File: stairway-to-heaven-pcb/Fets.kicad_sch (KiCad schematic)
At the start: 12 parts, among them Q1 FDN337N, Q2 FDN337N, Q3 FDN337N, Q4 FDN337N, Q5 FDN337N, Q6 FDN337N

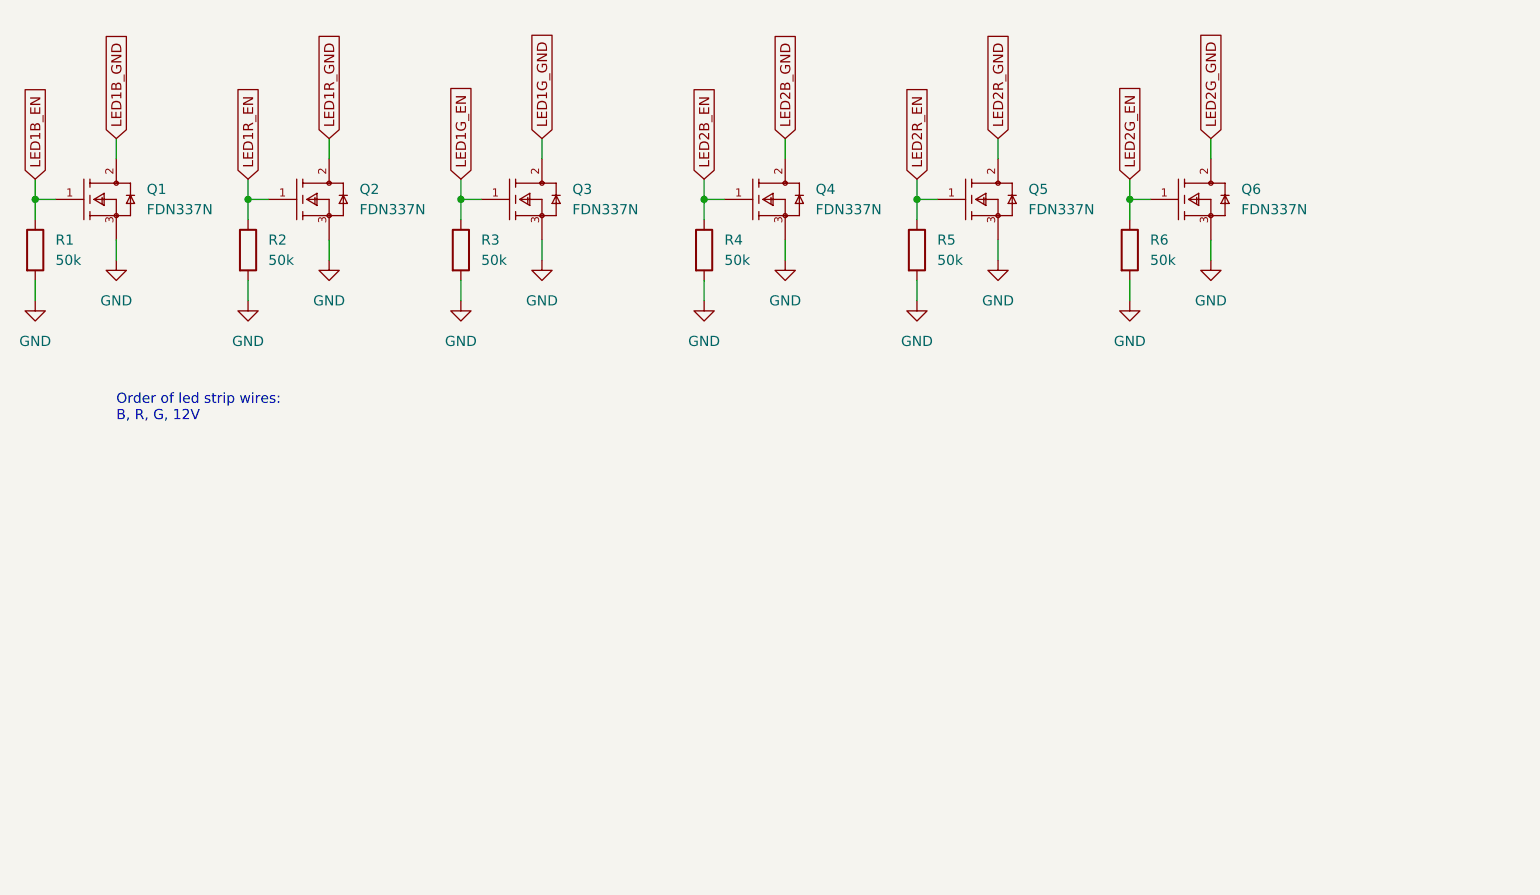
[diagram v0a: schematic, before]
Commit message: Psu, hierachical pages for fet driver
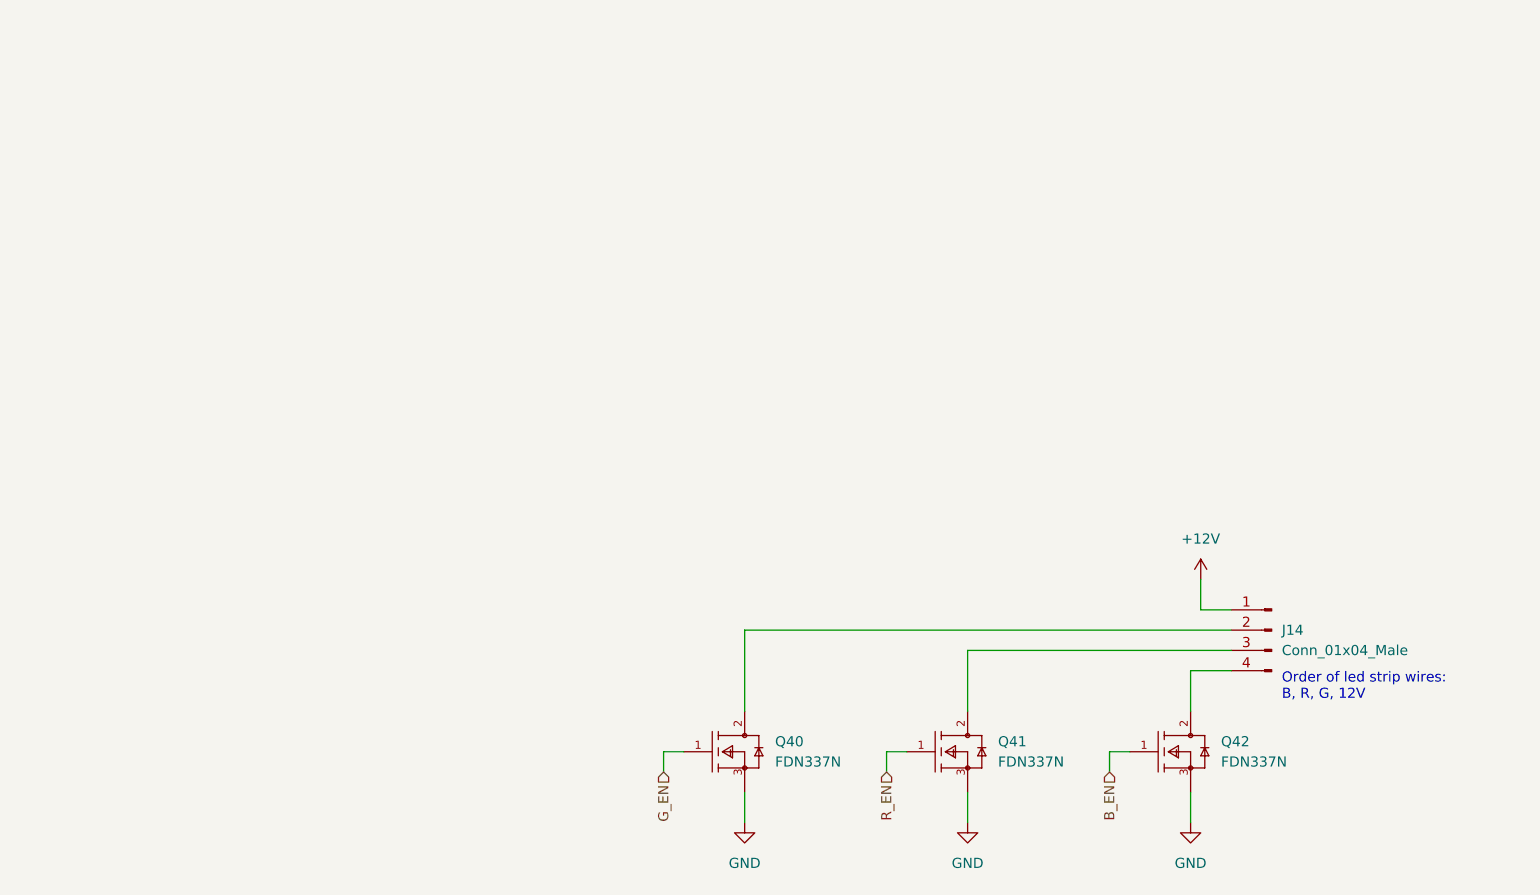
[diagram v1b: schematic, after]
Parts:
- removed Q1, Q2, Q3, Q4, Q5, Q6: FDN337N, FDN337N:ON_Semi-527AG-01-12_2008-O-IPC_B, symbol FDN337N:FDN337N
- removed R1, R2, R3, R4, R5, R6: 50k, Resistor_SMD:R_0805_2012Metric, symbol Device:R
- added J14: Conn_01x04_Male, Connector_PinHeader_2.54mm:PinHeader_1x04_P2.54mm_Vertical, symbol Connector:Conn_01x04_Male
- added Q40, Q41, Q42: FDN337N, FDN337N:ON_Semi-527AG-01-12_2008-O-IPC_B, symbol FDN337N:FDN337N
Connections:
- net GND: now also Q40.3 (S), Q41.3 (S), Q42.3 (S)
- new net: J14.2 (Pin_2), Q40.2 (D)
- new net: J14.4 (Pin_4), Q42.2 (D)
- new net: J14.3 (Pin_3), Q41.2 (D)
- new net +12V: J14.1 (Pin_1)
- new net B_EN: Q42.1 (G)
- new net G_EN: Q40.1 (G)
- new net R_EN: Q41.1 (G)

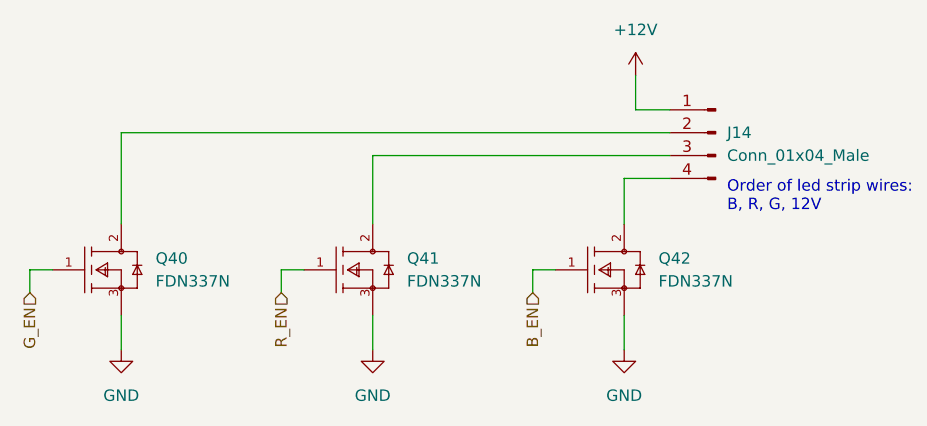
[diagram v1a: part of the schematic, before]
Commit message: initial pcb placement and routing tests
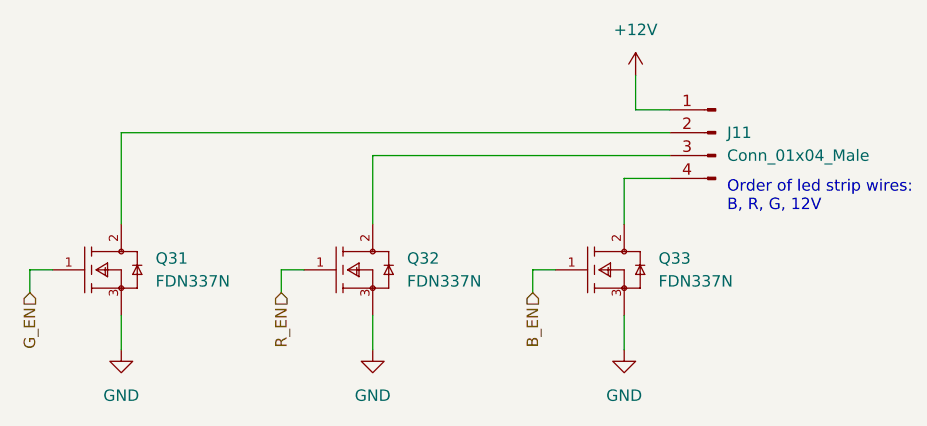
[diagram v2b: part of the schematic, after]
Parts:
- J11: renamed from J14; footprint Connector_PinHeader_2.54mm:PinHeader_1x04_P2.54mm_Vertical -> kicad-ss-libs:ScrewTerminal-5_08
- renumbered Q40 to Q31, Q41 to Q32, Q42 to Q33
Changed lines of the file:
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@@
   (symbol (lib_id "power:GND") (at 162.56 113.665 0)
     (in_bom yes) (on_board yes) (fields_autoplaced)
-    (property "Reference" "#PWR0157" (id 0) (at 162.56 120.015 0)
+    (property "Reference" "#PWR0145" (id 0) (at 162.56 120.015 0)
       (effects (font (size 1.27 1.27)) hide)
     )
@@
   (symbol (lib_id "FDN337N:FDN337N") (at 96.52 104.775 0)
     (in_bom yes) (on_board yes) (fields_autoplaced)
-    (property "Reference" "Q40" (id 0) (at 110.49 103.5049 0)
+    (property "Reference" "Q31" (id 0) (at 110.49 103.5049 0)
       (effects (font (size 1.27 1.27)) (justify left))
     )
@@
   (symbol (lib_id "FDN337N:FDN337N") (at 152.4 104.775 0)
     (in_bom yes) (on_board yes) (fields_autoplaced)
-    (property "Reference" "Q42" (id 0) (at 166.37 103.5049 0)
+    (property "Reference" "Q33" (id 0) (at 166.37 103.5049 0)
       (effects (font (size 1.27 1.27)) (justify left))
     )
@@
   (symbol (lib_id "power:GND") (at 134.62 113.665 0)
     (in_bom yes) (on_board yes) (fields_autoplaced)
-    (property "Reference" "#PWR0155" (id 0) (at 134.62 120.015 0)
+    (property "Reference" "#PWR0143" (id 0) (at 134.62 120.015 0)
       (effects (font (size 1.27 1.27)) hide)
     )
@@
   (symbol (lib_id "Connector:Conn_01x04_Male") (at 172.72 89.535 0) (mirror y)
     (in_bom yes) (on_board yes) (fields_autoplaced)
-    (property "Reference" "J14" (id 0) (at 173.99 89.5349 0)
+    (property "Reference" "J11" (id 0) (at 173.99 89.5349 0)
       (effects (font (size 1.27 1.27)) (justify right))
     )
@@
       (effects (font (size 1.27 1.27)) (justify right))
     )
-    (property "Footprint" "Connector_PinHeader_2.54mm:PinHeader_1x04_P2.54mm_Vertical" (id 2) (at 172.72 89.535 0)
+    (property "Footprint" "kicad-ss-libs:ScrewTerminal-5_08" (id 2) (at 172.72 89.535 0)
       (effects (font (size 1.27 1.27)) hide)
     )
@@
   (symbol (lib_id "FDN337N:FDN337N") (at 124.46 104.775 0)
     (in_bom yes) (on_board yes) (fields_autoplaced)
-    (property "Reference" "Q41" (id 0) (at 138.43 103.5049 0)
+    (property "Reference" "Q32" (id 0) (at 138.43 103.5049 0)
       (effects (font (size 1.27 1.27)) (justify left))
     )
@@
   (symbol (lib_id "power:GND") (at 106.68 113.665 0)
     (in_bom yes) (on_board yes) (fields_autoplaced)
-    (property "Reference" "#PWR0156" (id 0) (at 106.68 120.015 0)
+    (property "Reference" "#PWR0144" (id 0) (at 106.68 120.015 0)
       (effects (font (size 1.27 1.27)) hide)
     )
@@
   (symbol (lib_id "power:+12V") (at 163.83 83.185 0)
     (in_bom yes) (on_board yes) (fields_autoplaced)
-    (property "Reference" "#PWR0158" (id 0) (at 163.83 86.995 0)
-      (effects (font (size 1.27 1.27)) hide)
-    )
+    (property "Reference" "#PWR0146" (id 0) (at 163.83 86.995 0)
+      (effects (font (size 1.27 1.27)) hide)
+    )

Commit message: psu layout
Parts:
- renumbered J11 to J14, Q31 to Q40, Q32 to Q41, Q33 to Q42
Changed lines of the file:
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@@
   (symbol (lib_id "power:GND") (at 162.56 113.665 0)
     (in_bom yes) (on_board yes) (fields_autoplaced)
-    (property "Reference" "#PWR0145" (id 0) (at 162.56 120.015 0)
+    (property "Reference" "#PWR0157" (id 0) (at 162.56 120.015 0)
       (effects (font (size 1.27 1.27)) hide)
     )
@@
   (symbol (lib_id "FDN337N:FDN337N") (at 96.52 104.775 0)
     (in_bom yes) (on_board yes) (fields_autoplaced)
-    (property "Reference" "Q31" (id 0) (at 110.49 103.5049 0)
+    (property "Reference" "Q40" (id 0) (at 110.49 103.5049 0)
       (effects (font (size 1.27 1.27)) (justify left))
     )
@@
   (symbol (lib_id "FDN337N:FDN337N") (at 152.4 104.775 0)
     (in_bom yes) (on_board yes) (fields_autoplaced)
-    (property "Reference" "Q33" (id 0) (at 166.37 103.5049 0)
+    (property "Reference" "Q42" (id 0) (at 166.37 103.5049 0)
       (effects (font (size 1.27 1.27)) (justify left))
     )
@@
   (symbol (lib_id "power:GND") (at 134.62 113.665 0)
     (in_bom yes) (on_board yes) (fields_autoplaced)
-    (property "Reference" "#PWR0143" (id 0) (at 134.62 120.015 0)
+    (property "Reference" "#PWR0155" (id 0) (at 134.62 120.015 0)
       (effects (font (size 1.27 1.27)) hide)
     )
@@
   (symbol (lib_id "Connector:Conn_01x04_Male") (at 172.72 89.535 0) (mirror y)
     (in_bom yes) (on_board yes) (fields_autoplaced)
-    (property "Reference" "J11" (id 0) (at 173.99 89.5349 0)
+    (property "Reference" "J14" (id 0) (at 173.99 89.5349 0)
       (effects (font (size 1.27 1.27)) (justify right))
     )
@@
   (symbol (lib_id "FDN337N:FDN337N") (at 124.46 104.775 0)
     (in_bom yes) (on_board yes) (fields_autoplaced)
-    (property "Reference" "Q32" (id 0) (at 138.43 103.5049 0)
+    (property "Reference" "Q41" (id 0) (at 138.43 103.5049 0)
       (effects (font (size 1.27 1.27)) (justify left))
     )
@@
   (symbol (lib_id "power:GND") (at 106.68 113.665 0)
     (in_bom yes) (on_board yes) (fields_autoplaced)
-    (property "Reference" "#PWR0144" (id 0) (at 106.68 120.015 0)
+    (property "Reference" "#PWR0156" (id 0) (at 106.68 120.015 0)
       (effects (font (size 1.27 1.27)) hide)
     )
@@
   (symbol (lib_id "power:+12V") (at 163.83 83.185 0)
     (in_bom yes) (on_board yes) (fields_autoplaced)
-    (property "Reference" "#PWR0146" (id 0) (at 163.83 86.995 0)
-      (effects (font (size 1.27 1.27)) hide)
-    )
+    (property "Reference" "#PWR0158" (id 0) (at 163.83 86.995 0)
+      (effects (font (size 1.27 1.27)) hide)
+    )

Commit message: Vias galore
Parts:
- renumbered J14 to J4, Q40 to Q10, Q41 to Q11, Q42 to Q12
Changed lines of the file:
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@@
   (symbol (lib_id "power:GND") (at 162.56 113.665 0)
     (in_bom yes) (on_board yes) (fields_autoplaced)
-    (property "Reference" "#PWR0157" (id 0) (at 162.56 120.015 0)
+    (property "Reference" "#PWR0117" (id 0) (at 162.56 120.015 0)
       (effects (font (size 1.27 1.27)) hide)
     )
@@
   (symbol (lib_id "FDN337N:FDN337N") (at 96.52 104.775 0)
     (in_bom yes) (on_board yes) (fields_autoplaced)
-    (property "Reference" "Q40" (id 0) (at 110.49 103.5049 0)
+    (property "Reference" "Q10" (id 0) (at 110.49 103.5049 0)
       (effects (font (size 1.27 1.27)) (justify left))
     )
@@
   (symbol (lib_id "FDN337N:FDN337N") (at 152.4 104.775 0)
     (in_bom yes) (on_board yes) (fields_autoplaced)
-    (property "Reference" "Q42" (id 0) (at 166.37 103.5049 0)
+    (property "Reference" "Q12" (id 0) (at 166.37 103.5049 0)
       (effects (font (size 1.27 1.27)) (justify left))
     )
@@
   (symbol (lib_id "power:GND") (at 134.62 113.665 0)
     (in_bom yes) (on_board yes) (fields_autoplaced)
-    (property "Reference" "#PWR0155" (id 0) (at 134.62 120.015 0)
+    (property "Reference" "#PWR0115" (id 0) (at 134.62 120.015 0)
       (effects (font (size 1.27 1.27)) hide)
     )
@@
   (symbol (lib_id "Connector:Conn_01x04_Male") (at 172.72 89.535 0) (mirror y)
     (in_bom yes) (on_board yes) (fields_autoplaced)
-    (property "Reference" "J14" (id 0) (at 173.99 89.5349 0)
+    (property "Reference" "J4" (id 0) (at 173.99 89.5349 0)
       (effects (font (size 1.27 1.27)) (justify right))
     )
@@
   (symbol (lib_id "FDN337N:FDN337N") (at 124.46 104.775 0)
     (in_bom yes) (on_board yes) (fields_autoplaced)
-    (property "Reference" "Q41" (id 0) (at 138.43 103.5049 0)
+    (property "Reference" "Q11" (id 0) (at 138.43 103.5049 0)
       (effects (font (size 1.27 1.27)) (justify left))
     )
@@
   (symbol (lib_id "power:GND") (at 106.68 113.665 0)
     (in_bom yes) (on_board yes) (fields_autoplaced)
-    (property "Reference" "#PWR0156" (id 0) (at 106.68 120.015 0)
+    (property "Reference" "#PWR0116" (id 0) (at 106.68 120.015 0)
       (effects (font (size 1.27 1.27)) hide)
     )
@@
   (symbol (lib_id "power:+12V") (at 163.83 83.185 0)
     (in_bom yes) (on_board yes) (fields_autoplaced)
-    (property "Reference" "#PWR0158" (id 0) (at 163.83 86.995 0)
-      (effects (font (size 1.27 1.27)) hide)
-    )
+    (property "Reference" "#PWR0118" (id 0) (at 163.83 86.995 0)
+      (effects (font (size 1.27 1.27)) hide)
+    )

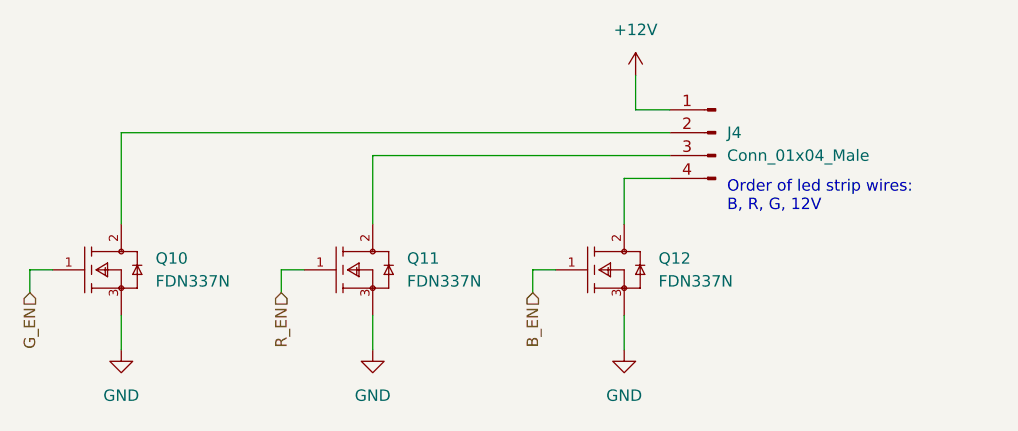
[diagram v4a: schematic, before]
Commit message: Pull-up resistors. Some sw work.
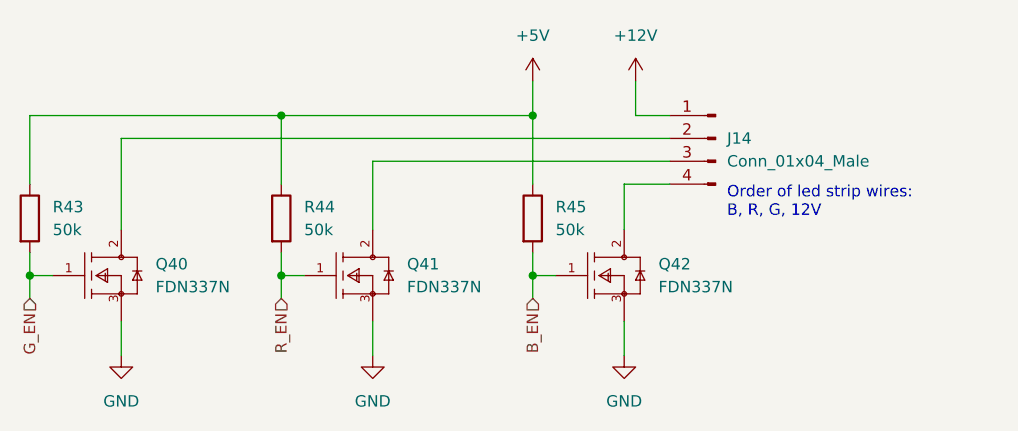
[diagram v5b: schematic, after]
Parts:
- added R43, R44, R45: 50k, Resistor_SMD:R_0805_2012Metric, symbol Device:R
- renumbered J4 to J14, Q10 to Q40, Q11 to Q41, Q12 to Q42
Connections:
- net B_EN: now also R45.2
- net G_EN: now also R43.2
- net R_EN: now also R44.2
- new net +5V: R43.1, R44.1, R45.1
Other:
- moved on the sheet: J14, Q40, Q41, Q42

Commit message: Silks, small mods
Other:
- title: (none) -> Stairway to Heaven
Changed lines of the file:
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@@
 (kicad_sch (version 20211123) (generator eeschema)
   (paper "A4")
+  (title_block
+    (title "Stairway to Heaven")
+  )
   (junction (at 124.46 105.41) (diameter 0) (color 0 0 0 0)
   )

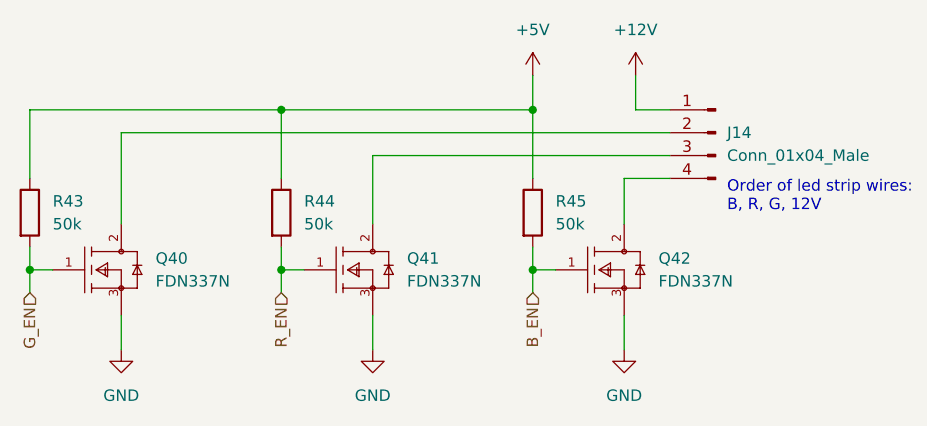
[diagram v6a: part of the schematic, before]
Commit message: Fix fet pullups to pulldowns
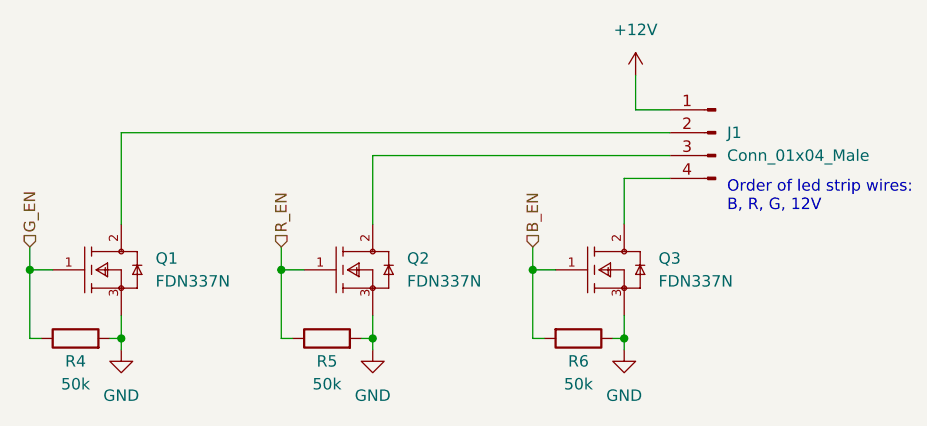
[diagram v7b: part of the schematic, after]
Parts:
- renumbered J14 to J1, Q40 to Q1, Q41 to Q2, Q42 to Q3, R43 to R4, R44 to R5, R45 to R6
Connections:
- net GND: now also R4.2, R5.2, R6.1
- net G_EN: now also R4.1; no longer R4.2
- net R_EN: now also R5.1; no longer R5.2
- removed net +5V: R4.1, R5.1, R6.1
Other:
- moved on the sheet: R4, R5, R6
